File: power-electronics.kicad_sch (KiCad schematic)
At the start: 2 parts

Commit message: add pss 3dmodels and testpoints
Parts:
- JP20001, JP20002: footprint (none) -> Jumper:SolderJumper-2_P1.3mm_Open_RoundedPad1.0x1.5mm
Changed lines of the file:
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@@
 			)
 		)
-		(property "Footprint" ""
+		(property "Footprint" "Jumper:SolderJumper-2_P1.3mm_Open_RoundedPad1.0x1.5mm"
 			(at 153.67 92.71 0)
 			(effects
@@
 			)
 		)
-		(property "Footprint" ""
+		(property "Footprint" "Jumper:SolderJumper-2_P1.3mm_Open_RoundedPad1.0x1.5mm"
 			(at 153.67 97.79 0)
 			(effects

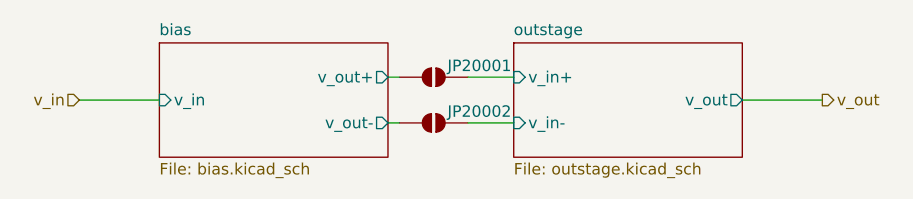
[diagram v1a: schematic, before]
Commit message: add outstage separation by connectors for individual PCB
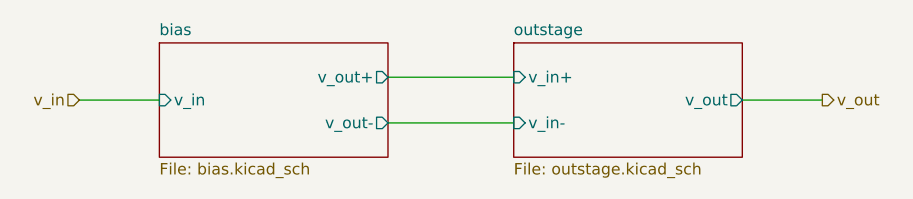
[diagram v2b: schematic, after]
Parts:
- removed JP20001, JP20002: SolderJumper_2_Open, Jumper:SolderJumper-2_P1.3mm_Open_RoundedPad1.0x1.5mm, symbol Jumper:SolderJumper_2_Open
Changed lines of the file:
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@@
-	(wire
-		(pts
-			(xy 157.48 92.71) (xy 162.56 92.71)
-		)
-		(stroke
-			(width 0)
-			(type default)
-		)
-	)
 	(wire
 		(pts
@@
 	(wire
 		(pts
-			(xy 157.48 97.79) (xy 162.56 97.79)
-		)
-		(stroke
-			(width 0)
-			(type default)
-		)
-	)
-	(wire
-		(pts
-			(xy 148.59 92.71) (xy 149.86 92.71)
+			(xy 148.59 92.71) (xy 162.56 92.71)
 		)
 		(stroke
@@
 	(wire
 		(pts
-			(xy 148.59 97.79) (xy 149.86 97.79)
+			(xy 148.59 97.79) (xy 162.56 97.79)
 		)
 		(stroke
@@
 		)
 	)
-	(symbol
-		(lib_id "Jumper:SolderJumper_2_Open")
-		(at 153.67 92.71 0)
-		(unit 1)
-		(exclude_from_sim yes)
-		(in_bom no)
-		(on_board yes)
-		(dnp no)
-		(property "Reference" "JP20001"
-			(at 158.75 91.44 0)
-			(effects
-				(font
-					(size 1.27 1.27)
-				)
-			)
-		)
-		(property "Value" "SolderJumper_2_Open"
-			(at 128.27 80.01 0)
-			(effects
-				(font
-					(size 1.27 1.27)
-				)
-				(hide yes)
-			)
-		)
-		(property "Footprint" "Jumper:SolderJumper-2_P1.3mm_Open_RoundedPad1.0x1.5mm"
-			(at 153.67 92.71 0)
-			(effects
-				(font
-					(size 1.27 1.27)
-				)
-				(hide yes)
-			)
-		)
-		(property "Datasheet" "~"
-			(at 153.67 92.71 0)
-			(effects
-				(font
-					(size 1.27 1.27)
-				)
-				(hide yes)
-			)
-		)
-		(property "Description" "Solder Jumper, 2-pole, open"
-			(at 153.67 92.71 0)
-			(effects
-				(font
-					(size 1.27 1.27)
-				)
-				(hide yes)
-			)
-		)
-		(pin "1"
-		)
-		(pin "2"
-		)
-		(instances
-			(project "pss"
-				(path "/3c438cf7-9350-4e9f-8115-1deba8984176/2f3feae7-a9ea-4cb9-8521-c9b88e99d2e7"
-					(reference "JP20001")
-					(unit 1)
-				)
-			)
-		)
-	)
-	(symbol
-		(lib_id "Jumper:SolderJumper_2_Open")
-		(at 153.67 97.79 0)
-		(unit 1)
-		(exclude_from_sim yes)
-		(in_bom no)
-		(on_board yes)
-		(dnp no)
-		(property "Reference" "JP20002"
-			(at 158.75 96.52 0)
-			(effects
-				(font
-					(size 1.27 1.27)
-				)
-			)
-		)
-		(property "Value" "SolderJumper_2_Open"
-			(at 128.27 85.09 0)
-			(effects
-				(font
-					(size 1.27 1.27)
-				)
-				(hide yes)
-			)
-		)
-		(property "Footprint" "Jumper:SolderJumper-2_P1.3mm_Open_RoundedPad1.0x1.5mm"
-			(at 153.67 97.79 0)
-			(effects
-				(font
-					(size 1.27 1.27)
-				)
-				(hide yes)
-			)
-		)
-		(property "Datasheet" "~"
-			(at 153.67 97.79 0)
-			(effects
-				(font
-					(size 1.27 1.27)
-				)
-				(hide yes)
-			)
-		)
-		(property "Description" "Solder Jumper, 2-pole, open"
-			(at 153.67 97.79 0)
-			(effects
-				(font
-					(size 1.27 1.27)
-				)
-				(hide yes)
-			)
-		)
-		(pin "1"
-		)
-		(pin "2"
-		)
-		(instances
-			(project "pss"
-				(path "/3c438cf7-9350-4e9f-8115-1deba8984176/2f3feae7-a9ea-4cb9-8521-c9b88e99d2e7"
-					(reference "JP20002")
-					(unit 1)
-				)
-			)
-		)
-	)
